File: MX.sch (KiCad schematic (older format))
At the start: 4 parts, among them SW1 MXSwitch

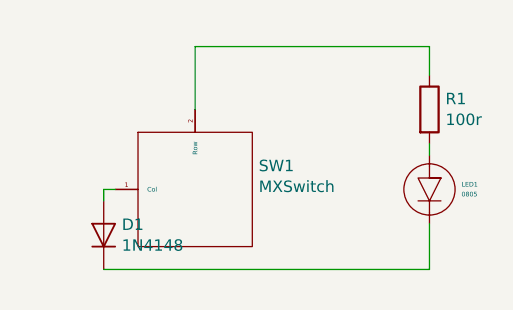
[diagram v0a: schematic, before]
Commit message: Added support for THT LEDs
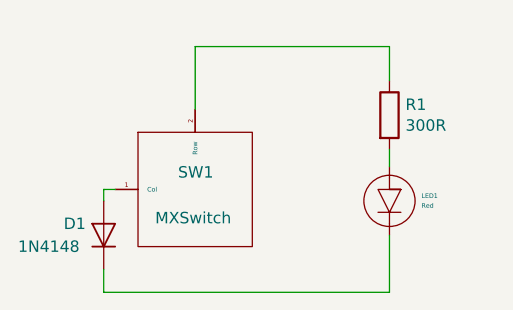
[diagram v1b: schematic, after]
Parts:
- D1: footprint Diode_THT:D_DO-15_P5.08mm_Vertical_AnodeUp -> Diode_THT:D_DO-35_SOD27_P7.62mm_Horizontal
- LED1: value 0805 -> Red
- R1: value 100r -> 300R
- SW1: footprint Keyboard_switches:MX700R -> Keyboard_switches:MX700H
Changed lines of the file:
@@
 U 1 1 5BFDA74A
 P 5025 2750
-F 0 "SW1" H 5303 2853 50  0000 L CNN
-F 1 "MXSwitch" H 5303 2762 50  0000 L CNN
-F 2 "Keyboard_switches:MX700R" H 5025 2750 50  0001 C CNN
+F 0 "SW1" H 4950 2825 50  0000 L CNN
+F 1 "MXSwitch" H 4850 2625 50  0000 L CNN
+F 2 "Keyboard_switches:MX700H" H 5025 2750 50  0001 C CNN
 F 3 "" H 5025 2750 50  0001 C CNN
 	1    5025 2750
@@
 $EndComp
 $Comp
-L Keyboard_switches:LED LED1
-U 1 1 5BFDA917
-P 6050 2750
-F 0 "LED1" V 6028 2890 20  0000 L CNN
-F 1 "0805" V 6071 2890 20  0000 L CNN
-F 2 "Keyboard_switches:smdLed0805" H 6050 2750 50  0001 C CNN
-F 3 "" H 6050 2750 50  0001 C CNN
-	1    6050 2750
-	0    1    1    0
-$EndComp
-$Comp
 L Device:D D1
 U 1 1 5BFDAC26
 P 4625 2950
-F 0 "D1" V 4671 2871 50  0000 R CNN
-F 1 "1N4148" V 4580 2871 50  0000 R CNN
-F 2 "Diode_THT:D_DO-15_P5.08mm_Vertical_AnodeUp" H 4625 2950 50  0001 C CNN
+F 0 "D1" V 4675 3125 50  0000 R CNN
+F 1 "1N4148" V 4575 3325 50  0000 R CNN
+F 2 "Diode_THT:D_DO-35_SOD27_P7.62mm_Horizontal" H 4625 2950 50  0001 C CNN
 F 3 "~" H 4625 2950 50  0001 C CNN
 	1    4625 2950
 	0    -1   -1   0
 $EndComp
-$Comp
-L Device:R R1
-U 1 1 5BFDAE7B
-P 6050 2400
-F 0 "R1" H 6120 2446 50  0000 L CNN
-F 1 "100r" H 6120 2355 50  0000 L CNN
-F 2 "Resistor_THT:R_Axial_DIN0204_L3.6mm_D1.6mm_P5.08mm_Horizontal" V 5980 2400 50  0001 C CNN
-F 3 "~" H 6050 2400 50  0001 C CNN
-	1    6050 2400
-	1    0    0    -1
-$EndComp
 Wire Wire Line
 	5025 2400 5025 2125
-Wire Wire Line
-	5025 2125 6050 2125
-Wire Wire Line
-	6050 2125 6050 2250
-Wire Wire Line
-	6050 2550 6050 2600
-Wire Wire Line
-	6050 2900 6050 3100
-Wire Wire Line
-	6050 3100 4625 3100
 Wire Wire Line
 	4675 2750 4625 2750
 Wire Wire Line
 	4625 2750 4625 2800
+Wire Wire Line
+	4625 3200 4625 3100
+$Comp
+L Device:R R1
+U 1 1 5BFDB5F4
+P 5875 2425
+F 0 "R1" H 5945 2471 50  0000 L CNN
+F 1 "300R" H 5945 2380 50  0000 L CNN
+F 2 "Resistor_THT:R_Axial_DIN0204_L3.6mm_D1.6mm_P5.08mm_Horizontal" V 5805 2425 50  0001 C CNN
+F 3 "~" H 5875 2425 50  0001 C CNN
+	1    5875 2425
+	1    0    0    -1
+$EndComp
+$Comp
+L Keyboard_switches:LED LED1
+U 1 1 5BFDB75A
+P 5875 2800
+F 0 "LED1" V 5853 2940 20  0000 L CNN
+F 1 "Red" V 5896 2940 20  0000 L CNN
+F 2 "Keyboard_switches:smdLed0805" H 5875 2800 50  0001 C CNN
+F 3 "" H 5875 2800 50  0001 C CNN
+	1    5875 2800
+	0    1    1    0
+$EndComp
+Wire Wire Line
+	5875 2125 5875 2275
+Wire Wire Line
+	5875 2575 5875 2650
+Wire Wire Line
+	5875 2950 5875 3200
+Wire Wire Line
+	5025 2125 5875 2125
+Wire Wire Line
+	4625 3200 5875 3200
 $EndSCHEMATC

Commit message: Improved silkscreen markings, LED footprints and added diode footprint
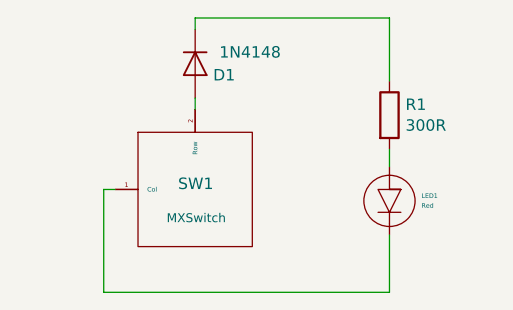
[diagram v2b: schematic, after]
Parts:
- D1: footprint Diode_THT:D_DO-35_SOD27_P7.62mm_Horizontal -> Keyboard_switches:thtDiode
- LED1: footprint Keyboard_switches:smdLed0805 -> Keyboard_switches:thtLED
- SW1: footprint Keyboard_switches:MX700H -> Keyboard_switches:MX100
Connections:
- net at D1.2 (A): now also SW1.2 (Row); no longer SW1.1 (Col)
- net at R1.1: now also D1.1 (K); no longer SW1.2 (Row)
- net at LED1.K: now also SW1.1 (Col); no longer D1.1 (K)
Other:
- moved on the sheet: D1
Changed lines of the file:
@@
 EESchema Schematic File Version 4
+LIBS:MX-cache
 EELAYER 26 0
 EELAYER END
@@
 $EndDescr
 $Comp
-L Keyboard_switches:MXSwitch SW1
-U 1 1 5BFDA74A
-P 5025 2750
-F 0 "SW1" H 4950 2825 50  0000 L CNN
-F 1 "MXSwitch" H 4850 2625 50  0000 L CNN
-F 2 "Keyboard_switches:MX700H" H 5025 2750 50  0001 C CNN
-F 3 "" H 5025 2750 50  0001 C CNN
-	1    5025 2750
-	1    0    0    -1
-$EndComp
-$Comp
 L Device:D D1
 U 1 1 5BFDAC26
-P 4625 2950
-F 0 "D1" V 4675 3125 50  0000 R CNN
-F 1 "1N4148" V 4575 3325 50  0000 R CNN
-F 2 "Diode_THT:D_DO-35_SOD27_P7.62mm_Horizontal" H 4625 2950 50  0001 C CNN
-F 3 "~" H 4625 2950 50  0001 C CNN
-	1    4625 2950
-	0    -1   -1   0
+P 5025 2200
+F 0 "D1" V 5075 2375 50  0000 R CNN
+F 1 "1N4148" V 4975 2575 50  0000 R CNN
+F 2 "Keyboard_switches:thtDiode" H 5025 2200 50  0001 C CNN
+F 3 "~" H 5025 2200 50  0001 C CNN
+	1    5025 2200
+	0    1    1    0
 $EndComp
 Wire Wire Line
-	5025 2400 5025 2125
-Wire Wire Line
 	4675 2750 4625 2750
-Wire Wire Line
-	4625 2750 4625 2800
-Wire Wire Line
-	4625 3200 4625 3100
 $Comp
 L Device:R R1
@@
 F 0 "LED1" V 5853 2940 20  0000 L CNN
 F 1 "Red" V 5896 2940 20  0000 L CNN
-F 2 "Keyboard_switches:smdLed0805" H 5875 2800 50  0001 C CNN
+F 2 "Keyboard_switches:thtLED" H 5875 2800 50  0001 C CNN
 F 3 "" H 5875 2800 50  0001 C CNN
 	1    5875 2800
@@
 $EndComp
 Wire Wire Line
-	5875 2125 5875 2275
-Wire Wire Line
 	5875 2575 5875 2650
 Wire Wire Line
 	5875 2950 5875 3200
 Wire Wire Line
-	5025 2125 5875 2125
+	4625 3200 5875 3200
+$Comp
+L Keyboard_switches:MXSwitch SW1
+U 1 1 5BFDCA5D
+P 5025 2750
+F 0 "SW1" H 4950 2775 50  0000 L CNN
+F 1 "MXSwitch" H 4900 2625 39  0000 L CNN
+F 2 "Keyboard_switches:MX100" H 5025 2750 50  0001 C CNN
+F 3 "" H 5025 2750 50  0001 C CNN
+	1    5025 2750
+	1    0    0    -1
+$EndComp
 Wire Wire Line
-	4625 3200 5875 3200
+	5025 2050 5025 2000
+Wire Wire Line
+	5025 2000 5875 2000
+Wire Wire Line
+	5875 2000 5875 2275
+Wire Wire Line
+	5025 2350 5025 2400
+Wire Wire Line
+	4625 2750 4625 3200
 $EndSCHEMATC
